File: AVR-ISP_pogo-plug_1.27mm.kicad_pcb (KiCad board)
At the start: 2 copper layers, 12 x 19 mm, 4 parts, among them P1 CONN_6, P2 CONN_6

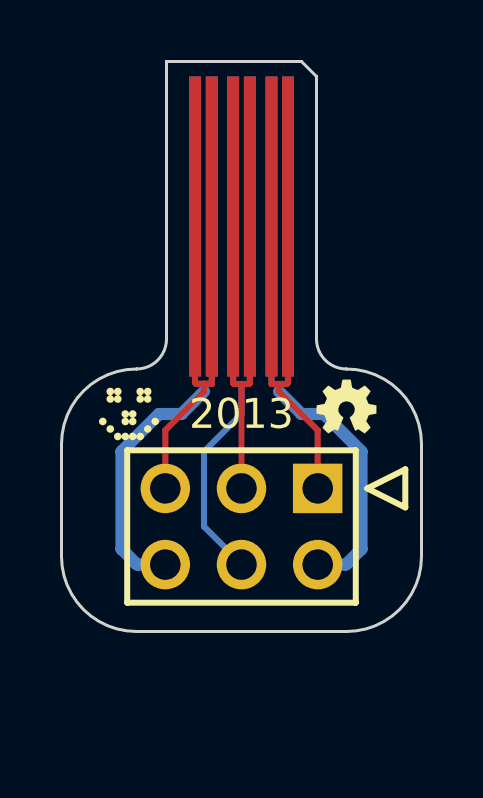
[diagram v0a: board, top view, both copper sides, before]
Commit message: Made it look more like a key.
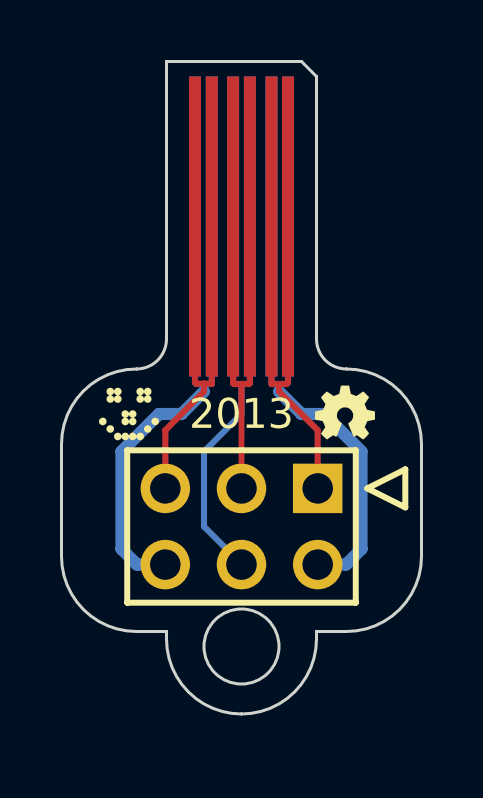
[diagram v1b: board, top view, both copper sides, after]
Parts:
- moved G2 0.21 mm to (72.0, 74.2)
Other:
- board size 12 x 19 mm -> 12 x 21.8 mm
- board text added: "KEY"
- board text added: "POGO"
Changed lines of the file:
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@@
     (links 12)
     (no_connects 0)
-    (area 62.449999 62.449999 74.550001 81.550001)
+    (area 62.169048 62.449999 75.347619 84.300001)
     (thickness 1.6)
-    (drawings 15)
+    (drawings 23)
     (tracks 59)
     (zones 0)
@@
     (mod_text_size 1.5 1.5)
     (mod_text_width 0.15)
-    (pad_size 0.4 10)
-    (pad_drill 0)
+    (pad_size 2 2)
+    (pad_drill 2)
     (pad_to_mask_clearance 0)
     (solder_mask_min_width 0.3)
@@
   )
   (module OSHW-logo_silkscreen_2mm (layer F.Cu)
-    (at 72 74)
+    (at 71.95 74.2)
     (fp_text reference G2 (at 0 1.05918) (layer F.SilkS) hide
       (effects (font (size 0.127 0.127) (thickness 0.01778)))
@@
       (xy 0.32766 -0.38354) (xy 0.35306 -0.37592) (xy 0.3556 -0.37592) (xy 0.381 -0.37338)) (layer F.SilkS) (width 0.00254))
   )
+  (gr_line (start 66 81.5) (end 66 81.75) (angle 90) (layer Edge.Cuts) (width 0.1))
+  (gr_line (start 71 81.5) (end 71 81.75) (angle 90) (layer Edge.Cuts) (width 0.1))
+  (gr_circle (center 68.5 82) (end 68.5 83.25) (layer Edge.Cuts) (width 0.1))
+  (gr_line (start 65 81.5) (end 66 81.5) (angle 90) (layer Edge.Cuts) (width 0.1))
+  (gr_line (start 71 81.5) (end 72 81.5) (angle 90) (layer Edge.Cuts) (width 0.1))
+  (gr_arc (start 68.5 81.75) (end 71 81.75) (angle 90) (layer Edge.Cuts) (width 0.1))
+  (gr_arc (start 68.5 81.75) (end 68.5 84.25) (angle 90) (layer Edge.Cuts) (width 0.1))
+  (gr_text POGO (at 73.2 77.75 270) (layer B.SilkS)
+    (effects (font (size 1 1) (thickness 0.2)) (justify mirror))
+  )
+  (gr_text KEY (at 63.65 77.75 270) (layer B.SilkS)
+    (effects (font (size 1 1) (thickness 0.2)) (justify mirror))
+  )
   (gr_text goo.gl/rwxuRB (at 68.55 74.2) (layer B.SilkS)
     (effects (font (size 1 0.9) (thickness 0.2)) (justify mirror))
@@
   (gr_line (start 70.5 62.5) (end 71 63) (angle 90) (layer Edge.Cuts) (width 0.1))
   (gr_line (start 66 71.75) (end 66 62.5) (angle 90) (layer Edge.Cuts) (width 0.1))
-  (gr_line (start 65 81.5) (end 72 81.5) (angle 90) (layer Edge.Cuts) (width 0.1))
   (gr_arc (start 65 71.75) (end 66 71.75) (angle 90) (layer Edge.Cuts) (width 0.1))
   (gr_arc (start 72 71.75) (end 72 72.75) (angle 90) (layer Edge.Cuts) (width 0.1))

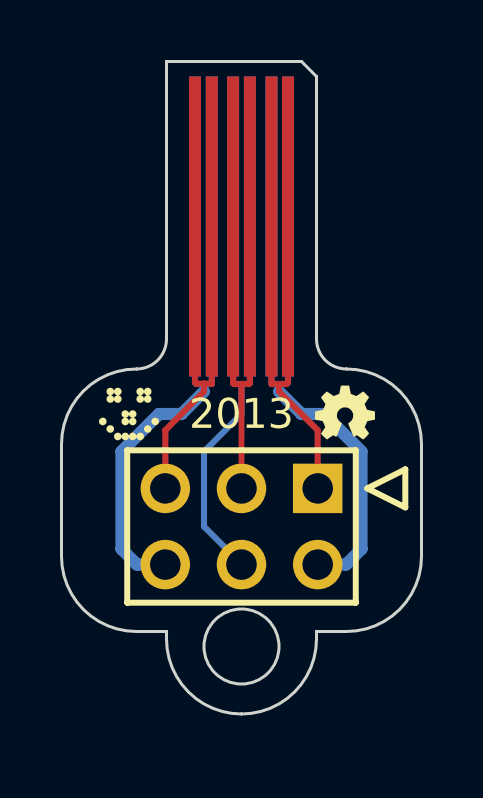
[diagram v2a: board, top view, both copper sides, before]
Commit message: Board outline tweaks.
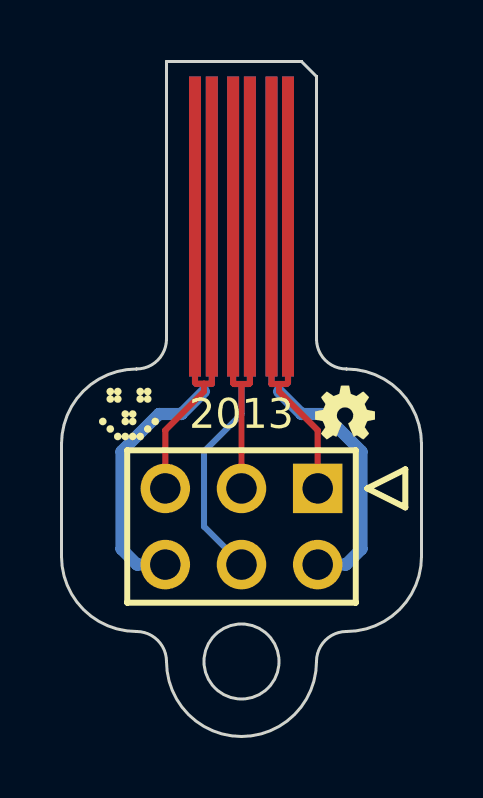
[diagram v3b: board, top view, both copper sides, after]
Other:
- board size 12 x 21.8 mm -> 12 x 22.5 mm
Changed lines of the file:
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@@
-(kicad_pcb (version 3) (host pcbnew "(2013-10-07 BZR 4378)-product")
+(kicad_pcb (version 3) (host pcbnew "(2013-10-11 BZR 4379)-product")
   (general
     (links 12)
@@
     (area 62.169048 62.449999 75.347619 84.300001)
     (thickness 1.6)
-    (drawings 23)
+    (drawings 20)
     (tracks 59)
     (zones 0)
@@
       (xy 0.32766 -0.38354) (xy 0.35306 -0.37592) (xy 0.3556 -0.37592) (xy 0.381 -0.37338)) (layer F.SilkS) (width 0.00254))
   )
-  (gr_line (start 66 81.5) (end 66 81.75) (angle 90) (layer Edge.Cuts) (width 0.1))
-  (gr_line (start 71 81.5) (end 71 81.75) (angle 90) (layer Edge.Cuts) (width 0.1))
-  (gr_circle (center 68.5 82) (end 68.5 83.25) (layer Edge.Cuts) (width 0.1))
-  (gr_line (start 65 81.5) (end 66 81.5) (angle 90) (layer Edge.Cuts) (width 0.1))
-  (gr_line (start 71 81.5) (end 72 81.5) (angle 90) (layer Edge.Cuts) (width 0.1))
-  (gr_arc (start 68.5 81.75) (end 71 81.75) (angle 90) (layer Edge.Cuts) (width 0.1))
-  (gr_arc (start 68.5 81.75) (end 68.5 84.25) (angle 90) (layer Edge.Cuts) (width 0.1))
+  (gr_arc (start 68.5 82.5) (end 71 82.5) (angle 180) (layer Edge.Cuts) (width 0.1))
+  (gr_arc (start 65 82.5) (end 65 81.5) (angle 90) (layer Edge.Cuts) (width 0.1))
+  (gr_arc (start 72 82.5) (end 71 82.5) (angle 90) (layer Edge.Cuts) (width 0.1))
+  (gr_circle (center 68.5 82.5) (end 68.5 83.75) (layer Edge.Cuts) (width 0.1))
   (gr_text POGO (at 73.2 77.75 270) (layer B.SilkS)
     (effects (font (size 1 1) (thickness 0.2)) (justify mirror))
